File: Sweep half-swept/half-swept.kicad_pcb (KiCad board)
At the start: 2 copper layers, 108.9 x 86.3 mm, 25 parts, among them J2 AudioJack4dpb, SW1 SW_Push, SW10 SW_Push, SW11 SW_Push, SW12 SW_Push, SW13 SW_Push, SW14 SW_Push, SW15 SW_Push, SW16 SW_Push, SW17 SW_Push, SW2 SW_Push, SW3 SW_Push, SW4 SW_Push, SW5 SW_Push, SW6 SW_Push, SW7 SW_Push, SW8 SW_Push, SW9 SW_Push, U1 ProMicro-kbd

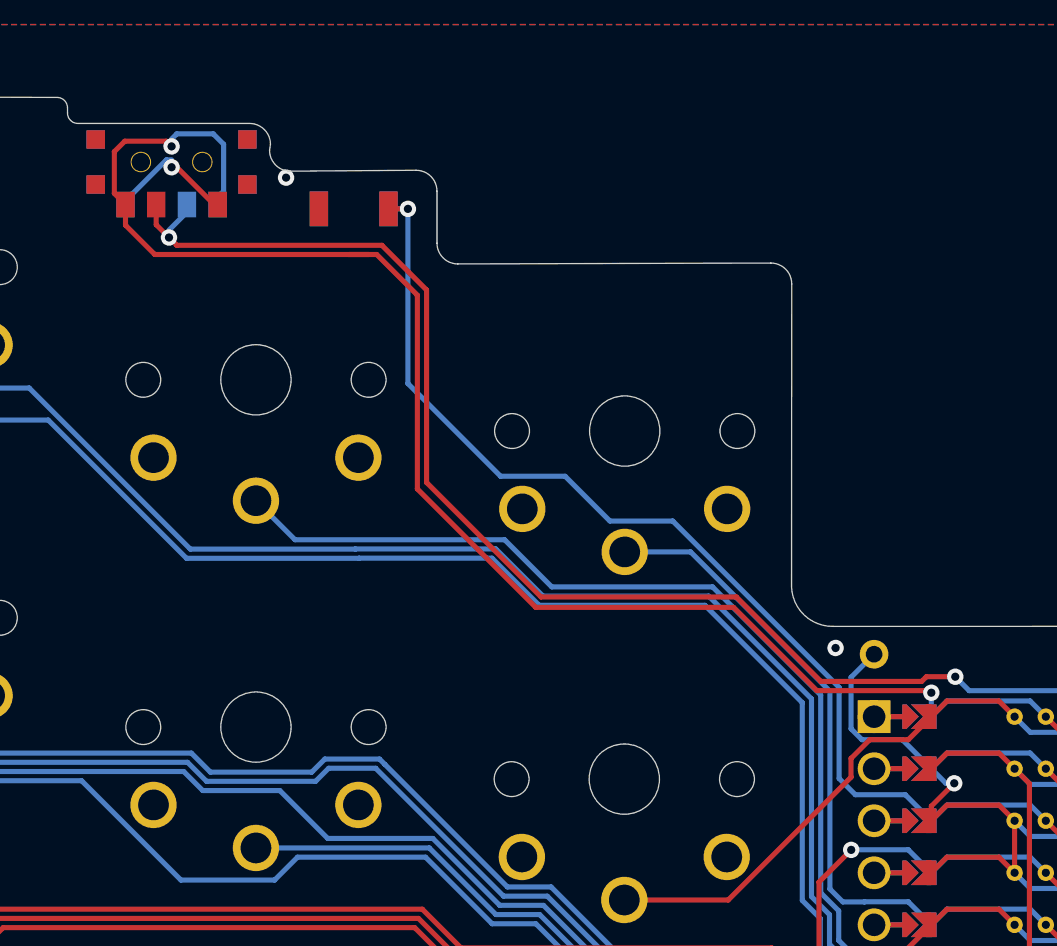
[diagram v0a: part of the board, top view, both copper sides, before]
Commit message: Tweaks to satisfy the Design Rules Checker
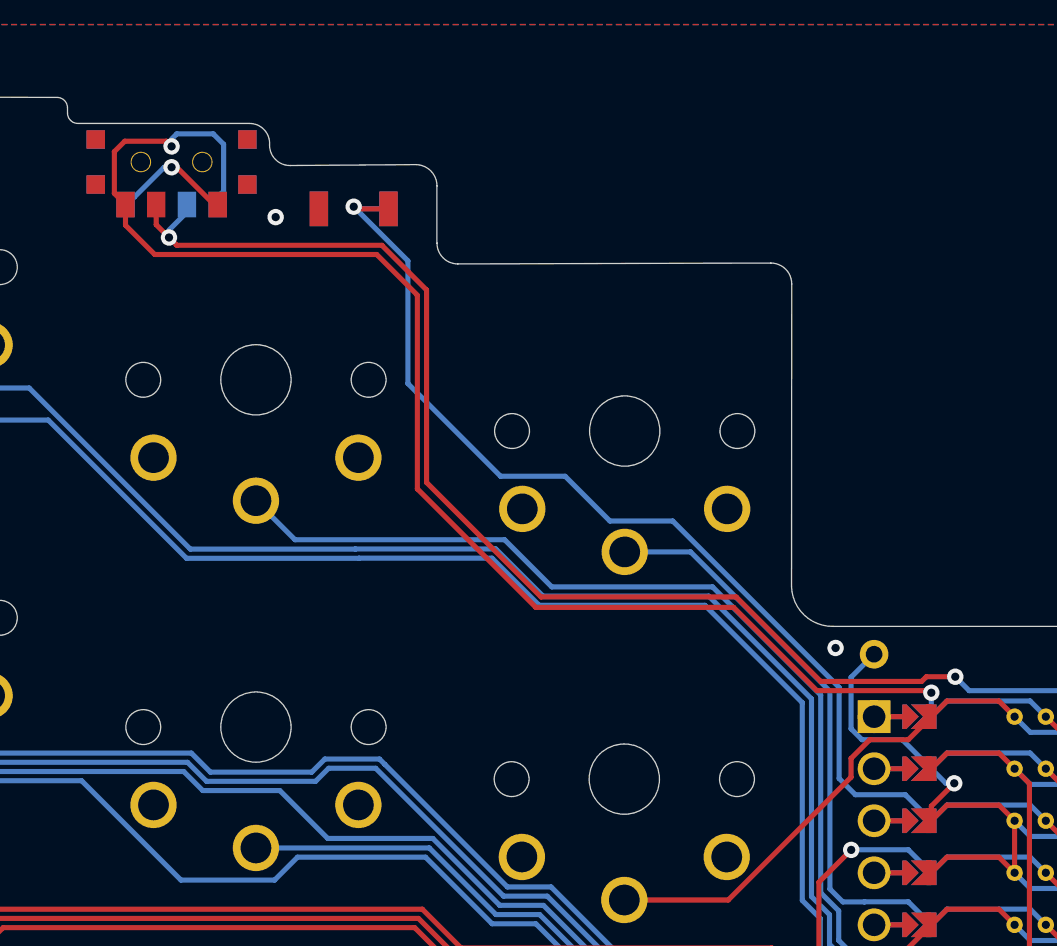
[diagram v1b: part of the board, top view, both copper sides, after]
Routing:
- net reset: track 47.6 -> 50.2 mm
- net raw: track 69.0 -> 68.0 mm
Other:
- outline, holes or cut-outs redrawn

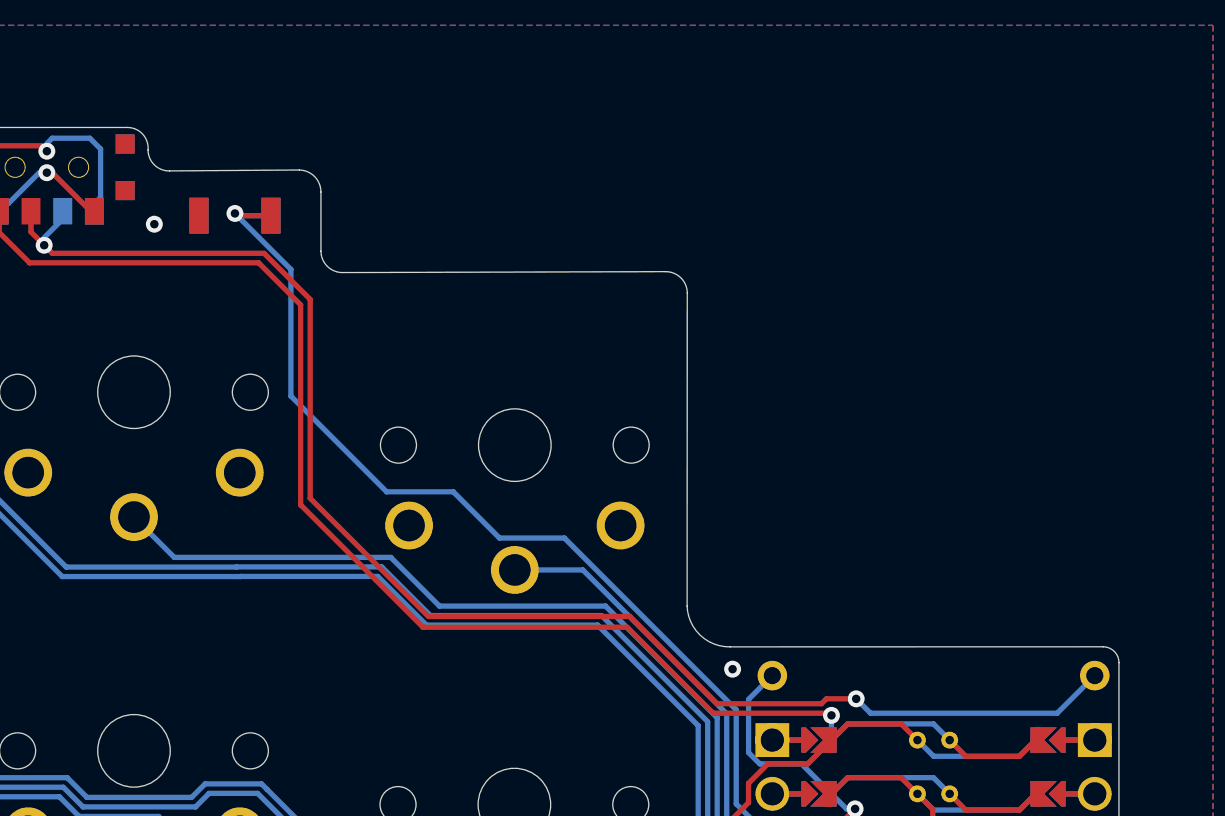
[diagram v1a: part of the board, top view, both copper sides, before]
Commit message: Added more separation between the reset button and the switch below
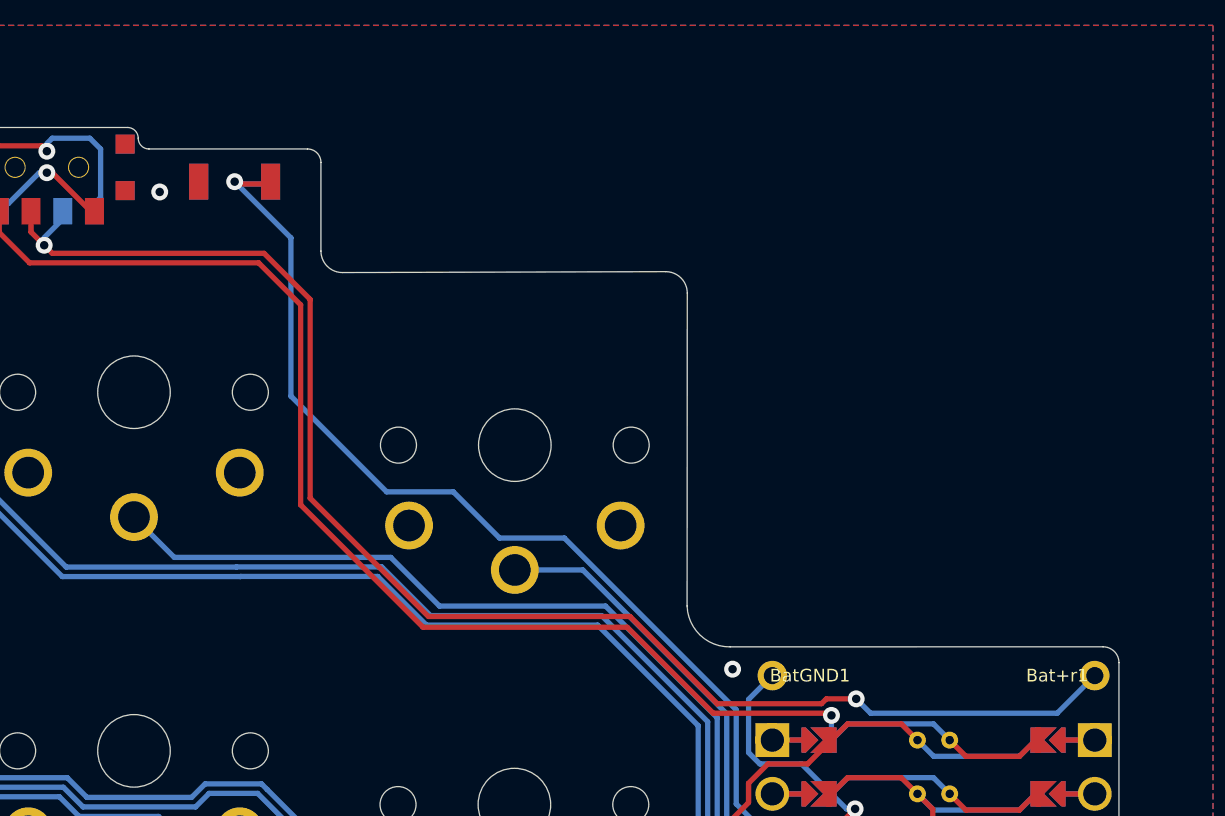
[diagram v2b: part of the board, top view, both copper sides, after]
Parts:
- Bat+r1, BatGND1: renamed from  
- moved RSW2 1.61 mm to (85.8, 22.6)
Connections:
- RSW2 pad 1: gnd -> reset
- RSW2 pad 2: gnd -> reset
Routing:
- net reset: track 50.2 -> 51.7 mm
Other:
- outline, holes or cut-outs redrawn
